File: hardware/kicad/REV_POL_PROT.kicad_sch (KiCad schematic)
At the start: 0 parts

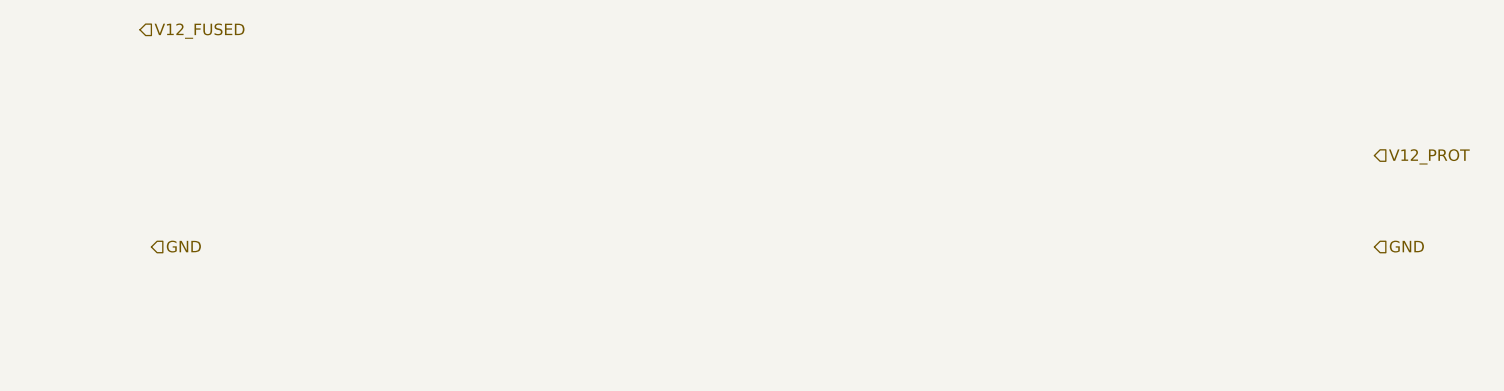
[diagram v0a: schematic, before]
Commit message: feat: implemented keypad & reverse polarity protection
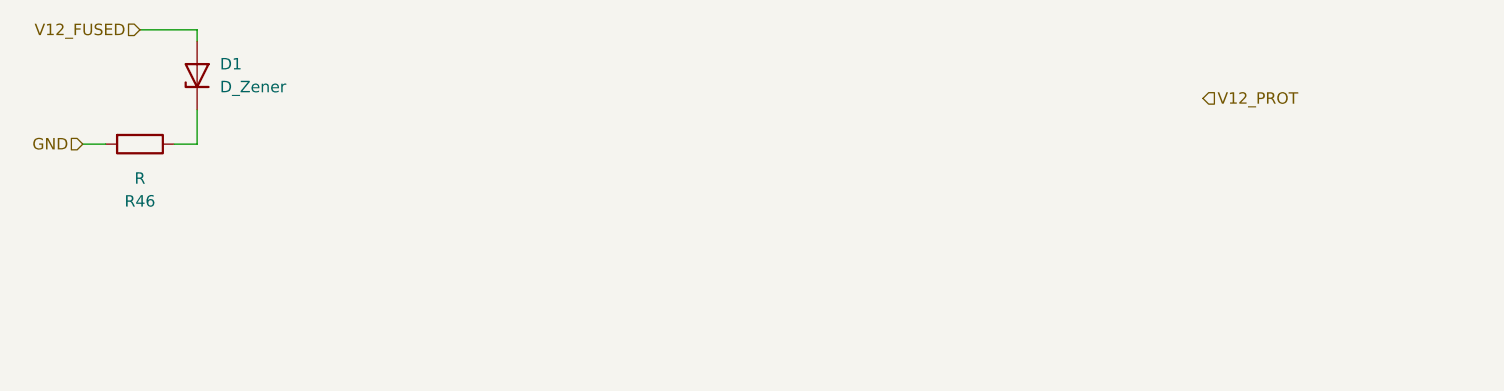
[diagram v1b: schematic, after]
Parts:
- added D1: D_Zener, symbol Device:D_Zener
- added R46: R, symbol Device:R
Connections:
- net GND: now also R46.2
- net V12_FUSED: now also D1.2 (A)
- new net: D1.1 (K), R46.1
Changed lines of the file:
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@@
 	(generator_version "9.0")
 	(paper "A4")
+	(wire
+		(pts
+			(xy 62.23 81.28) (xy 59.69 81.28)
+		)
+		(stroke
+			(width 0)
+			(type default)
+		)
+	)
+	(wire
+		(pts
+			(xy 55.88 68.58) (xy 62.23 68.58)
+		)
+		(stroke
+			(width 0)
+			(type default)
+		)
+	)
+	(wire
+		(pts
+			(xy 62.23 68.58) (xy 62.23 69.85)
+		)
+		(stroke
+			(width 0)
+			(type default)
+		)
+	)
+	(wire
+		(pts
+			(xy 49.53 81.28) (xy 52.07 81.28)
+		)
+		(stroke
+			(width 0)
+			(type default)
+		)
+	)
+	(wire
+		(pts
+			(xy 62.23 77.47) (xy 62.23 81.28)
+		)
+		(stroke
+			(width 0)
+			(type default)
+		)
+	)
 	(hierarchical_label "V12_FUSED"
 		(shape input)
-		(at 55.88 68.58 0)
+		(at 55.88 68.58 180)
 		(effects
 			(font
 				(size 1.27 1.27)
 			)
-			(justify left)
+			(justify right)
 		)
 	)
 	(hierarchical_label "GND"
 		(shape input)
-		(at 57.15 92.71 0)
+		(at 49.53 81.28 180)
 		(effects
 			(font
 				(size 1.27 1.27)
 			)
-			(justify left)
+			(justify right)
 		)
 	)
 	(hierarchical_label "V12_PROT"
 		(shape input)
-		(at 193.04 82.55 0)
+		(at 173.99 76.2 0)
 		(effects
 			(font
@@
 		)
 	)
-	(hierarchical_label "GND"
-		(shape input)
-		(at 193.04 92.71 0)
-		(effects
-			(font
-				(size 1.27 1.27)
-			)
-			(justify left)
-		)
-	)
+	(symbol
+		(lib_id "Device:R")
+		(at 55.88 81.28 270)
+		(unit 1)
+		(exclude_from_sim no)
+		(in_bom yes)
+		(on_board yes)
+		(dnp no)
+		(property "Reference" "R46"
+			(at 55.88 87.63 90)
+			(effects
+				(font
+					(size 1.27 1.27)
+				)
+			)
+		)
+		(property "Value" "R"
+			(at 55.88 85.09 90)
+			(effects
+				(font
+					(size 1.27 1.27)
+				)
+			)
+		)
+		(property "Footprint" ""
+			(at 55.88 79.502 90)
+			(effects
+				(font
+					(size 1.27 1.27)
+				)
+				(hide yes)
+			)
+		)
+		(property "Datasheet" "~"
+			(at 55.88 81.28 0)
+			(effects
+				(font
+					(size 1.27 1.27)
+				)
+				(hide yes)
+			)
+		)
+		(property "Description" "Resistor"
+			(at 55.88 81.28 0)
+			(effects
+				(font
+					(size 1.27 1.27)
+				)
+				(hide yes)
+			)
+		)
+		(pin "2"
+		)
+		(pin "1"
+		)
+		(instances
+			(project ""
+				(path "/0357579f-0f06-4880-b651-8e2778a9baa9/2731e8ed-07c3-48e2-8ff5-054edae4aa44/5139d80d-345d-42bc-baee-655042eeaf97"
+					(reference "R46")
+					(unit 1)
+				)
+			)
+		)
+	)
+	(symbol
+		(lib_id "Device:D_Zener")
+		(at 62.23 73.66 90)
+		(unit 1)
+		(exclude_from_sim no)
+		(in_bom yes)
+		(on_board yes)
+		(dnp no)
+		(fields_autoplaced yes)
+		(property "Reference" "D1"
+			(at 64.77 72.3899 90)
+			(effects
+				(font
+					(size 1.27 1.27)
+				)
+				(justify right)
+			)
+		)
+		(property "Value" "D_Zener"
+			(at 64.77 74.9299 90)
+			(effects
+				(font
+					(size 1.27 1.27)
+				)
+				(justify right)
+			)
+		)
+		(property "Footprint" ""
+			(at 62.23 73.66 0)
+			(effects
+				(font
+					(size 1.27 1.27)
+				)
+				(hide yes)
+			)
+		)
+		(property "Datasheet" "~"
+			(at 62.23 73.66 0)
+			(effects
+				(font
+					(size 1.27 1.27)
+				)
+				(hide yes)
+			)
+		)
+		(property "Description" "Zener diode"
+			(at 62.23 73.66 0)
+			(effects
+				(font
+					(size 1.27 1.27)
+				)
+				(hide yes)
+			)
+		)
+		(pin "2"
+		)
+		(pin "1"
+		)
+		(instances
+			(project ""
+				(path "/0357579f-0f06-4880-b651-8e2778a9baa9/2731e8ed-07c3-48e2-8ff5-054edae4aa44/5139d80d-345d-42bc-baee-655042eeaf97"
+					(reference "D1")
+					(unit 1)
+				)
+			)
+		)
+	)

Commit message: fix: error fixing & connection config
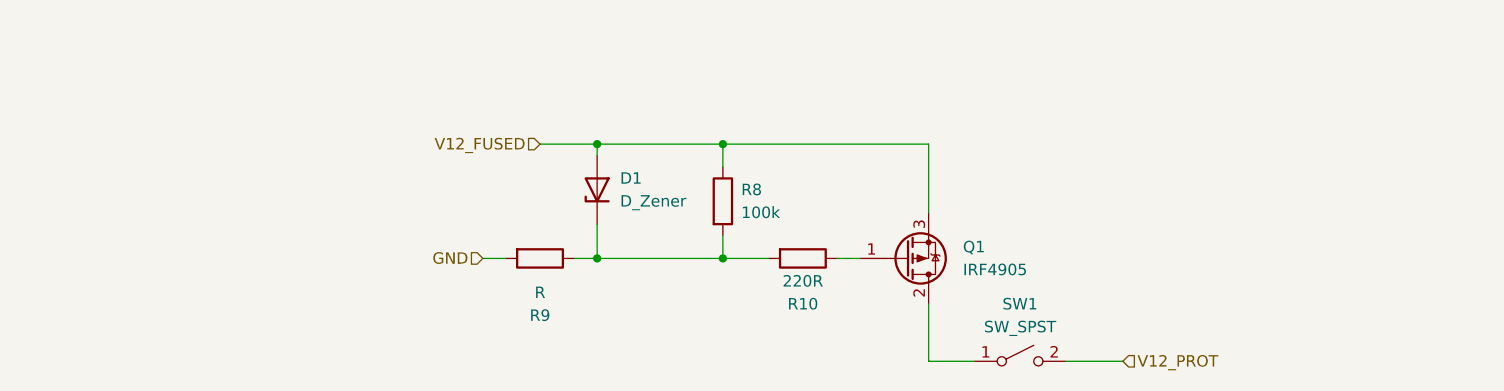
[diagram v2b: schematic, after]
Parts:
- added Q1: IRF4905, Package_TO_SOT_THT:TO-220-3_Vertical, symbol Transistor_FET:IRF4905
- added R10: 220R, symbol Device:R
- added R8: 100k, symbol Device:R
- added SW1: SW_SPST, symbol Switch:SW_SPST
- renumbered R46 to R9
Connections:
- net V12_FUSED: now also Q1.3 (S), R8.1
- net V12_PROT: now also SW1.2 (B)
- net at D1.1 (K), R9.1: now also R10.2, R8.2
- new net: Q1.1 (G), R10.1
- new net: Q1.2 (D), SW1.1 (A)
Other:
- moved on the sheet: D1, R9

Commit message: docs: added end semester report for project
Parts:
- D1: symbol Device:D_Zener -> TPSM82903:D_Zener
- Q1: symbol Transistor_FET:IRF4905 -> TPSM82903:IRF4905
- R10, R8, R9: symbol Device:R -> TPSM82903:R
- SW1: symbol Switch:SW_SPST -> TPSM82903:SW_SPST
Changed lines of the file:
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@@
 	)
 	(symbol
-		(lib_id "Device:R")
+		(lib_id "TPSM82903:R")
 		(at 100.33 93.98 270)
 		(unit 1)
@@
 	)
 	(symbol
-		(lib_id "Device:R")
+		(lib_id "TPSM82903:R")
 		(at 129.54 93.98 270)
 		(unit 1)
@@
 	)
 	(symbol
-		(lib_id "Device:R")
+		(lib_id "TPSM82903:R")
 		(at 120.65 87.63 0)
 		(unit 1)
@@
 	)
 	(symbol
-		(lib_id "Switch:SW_SPST")
+		(lib_id "TPSM82903:SW_SPST")
 		(at 153.67 105.41 0)
 		(unit 1)
@@
 	)
 	(symbol
-		(lib_id "Device:D_Zener")
+		(lib_id "TPSM82903:D_Zener")
 		(at 106.68 86.36 90)
 		(unit 1)
@@
 	)
 	(symbol
-		(lib_id "Transistor_FET:IRF4905")
+		(lib_id "TPSM82903:IRF4905")
 		(at 140.97 93.98 0)
 		(mirror x)
